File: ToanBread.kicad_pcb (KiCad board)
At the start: 2 copper layers, 53.3 x 101.6 mm, 32 parts, among them J1 PJ-059A, J2 AUDIO_IN, J3 VBIAS_OUT, J4 9V_OUT, J5 AUDIO_OUT, J6 EFF_OUT, J7 EFF_IN, U1 LM4562NA

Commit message: First pass at pcb layout
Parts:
- moved R6 59.3 mm to (134.6, 127.0), turned to 180 degrees
- moved C1 50.8 mm to (132.1, 114.3)
- moved C2 45.7 mm to (132.1, 61.0)
- moved C6 45.7 mm to (160.0, 78.7)
- moved J6 45.7 mm to (132.1, 50.8)
- moved J7 45.7 mm to (160.0, 50.8)
- moved R10 45.7 mm to (149.9, 68.6)
- moved R2 45.7 mm to (149.9, 91.4)
- moved R8 45.7 mm to (149.9, 86.4)
- moved S1 45.7 mm to (132.3, 137.2)
- moved BT1 45.7 mm to (121.9, 58.4)
- moved C4 45.7 mm to (134.6, 86.4)
- moved C5 45.7 mm to (165.1, 88.9)
- moved D1 45.7 mm to (124.5, 121.9)
- moved D3 45.7 mm to (152.4, 61.0)
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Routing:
- net BUF2_{OUT}: track 0.00 -> 84.1 mm
- net Net-(BT1--): track 0.00 -> 63.0 mm
- net BUF1_{IN}: track 0.00 -> 56.4 mm
- net Net-(J7-Pin_1): track 0.00 -> 54.2 mm
- net SIG: track 0.00 -> 49.1 mm
- net Net-(J6-Pin_1): track 0.00 -> 43.5 mm
- net Net-(R10-Pad2): track 0.00 -> 31.1 mm
- net Net-(J5-Pad2): track 0.00 -> 29.0 mm
- net Net-(R7-Pad1): track 0.00 -> 22.3 mm
- net Net-(C2-Pad1): track 0.00 -> 21.3 mm
- net Net-(D1-K): track 0.00 -> 21.1 mm
- net Net-(BT1-+): track 0.00 -> 20.0 mm
- net Net-(C4-Pad2): track 0.00 -> 16.9 mm
- net Net-(J3-Pin_2): track 0.00 -> 16.2 mm
- net 4V5: track 0.00 -> 15.2 mm
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- added copper zone on B.Cu, net GND
- added copper zone on F.Cu, net GND
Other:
- board size 53.3 x 101.6 mm -> 53.3 x 99.1 mm

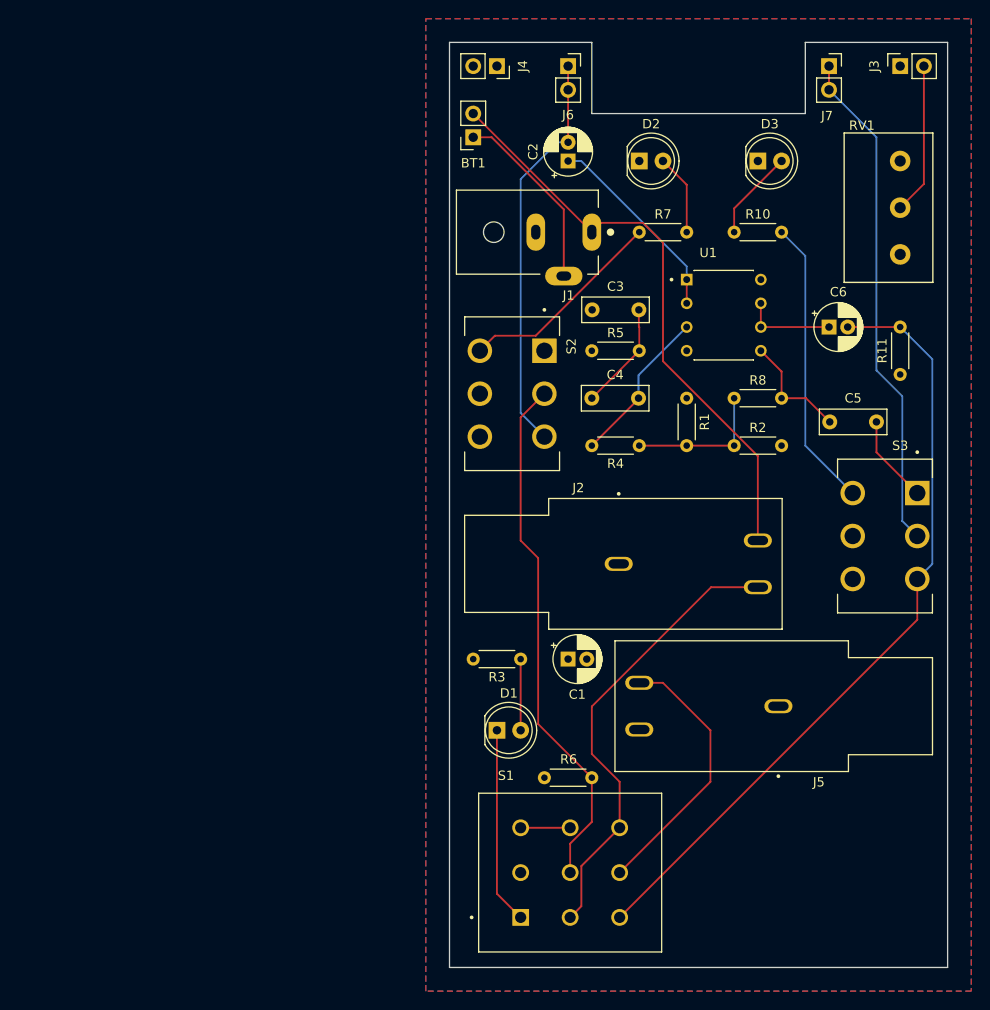
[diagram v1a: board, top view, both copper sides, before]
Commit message: Add info and logo to silkscreen
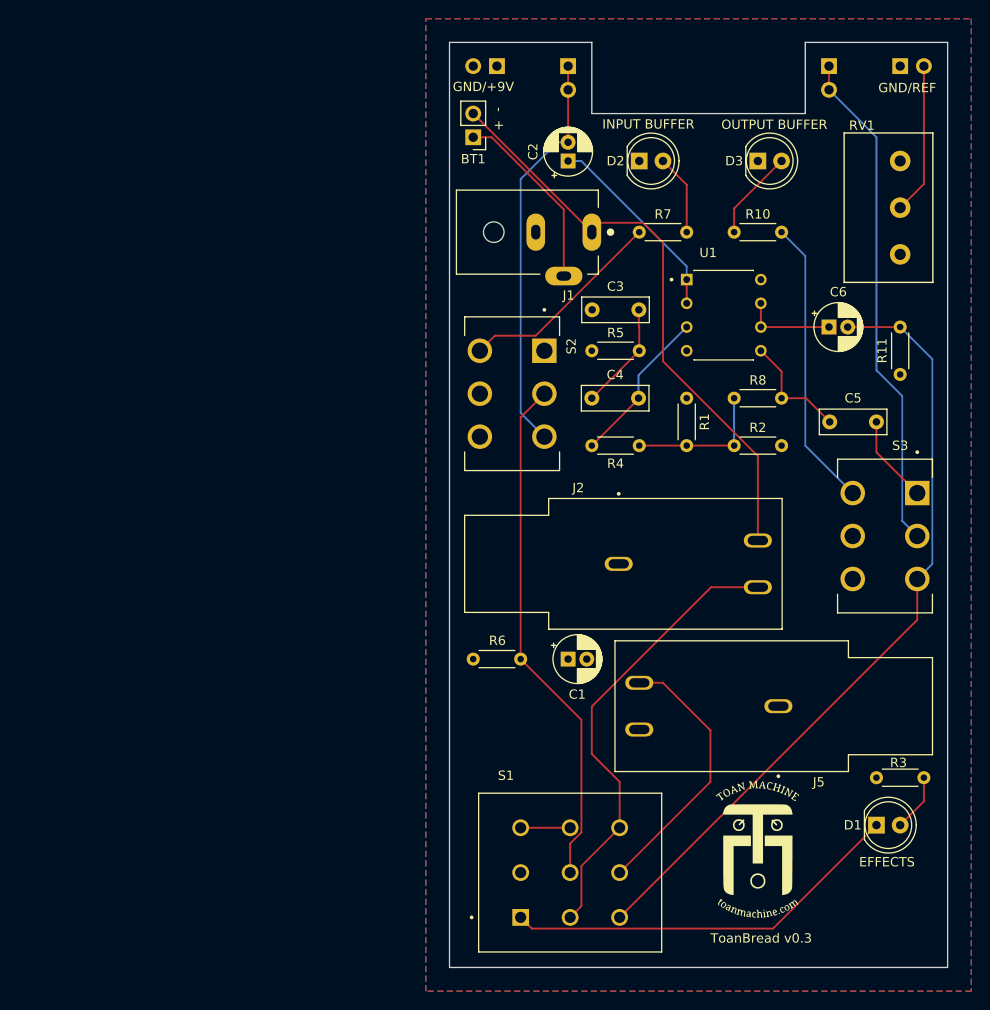
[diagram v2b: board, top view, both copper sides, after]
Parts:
- added G***: LOGO, ProjectSpecific:ToanMachineLogo, F.Cu at (152.4, 134.6)
- BT1: footprint Connector_PinSocket_2.54mm:PinSocket_1x02_P2.54mm_Vertical -> Connector_PinHeader_2.54mm:PinHeader_1x02_P2.54mm_Vertical
- J3, J4, J6, J7: footprint Connector_PinSocket_2.54mm:PinSocket_1x02_P2.54mm_Vertical -> Connector_PinHeader_2.54mm:PinHeader_1x02_P2.54mm_Vertical; moved to B.Cu
- moved R3 45.0 mm to (170.2, 127.0)
- moved D1 41.9 mm to (165.1, 132.1)
- moved R6 14.8 mm to (127.0, 114.3)
- turned J3 to -90 degrees
- turned J4 to 90 degrees
- turned J6 to 180 degrees
- turned J7 to 180 degrees
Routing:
- net Net-(D1-K): track 21.1 -> 43.2 mm
- net Net-(D1-A): track 7.62 -> 6.13 mm
- net BUF1_{IN}: track 56.4 -> 55.5 mm
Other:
- board text added: "- +"
- board text added: "EFFECTS"
- board text added: "GND/+9V"
- board text added: "GND/REF"
- board text added: "INPUT BUFFER"
- board text added: "OUTPUT BUFFER"
- board text added: "ToanBread v0.3"

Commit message: Final updates to the v0.3 board
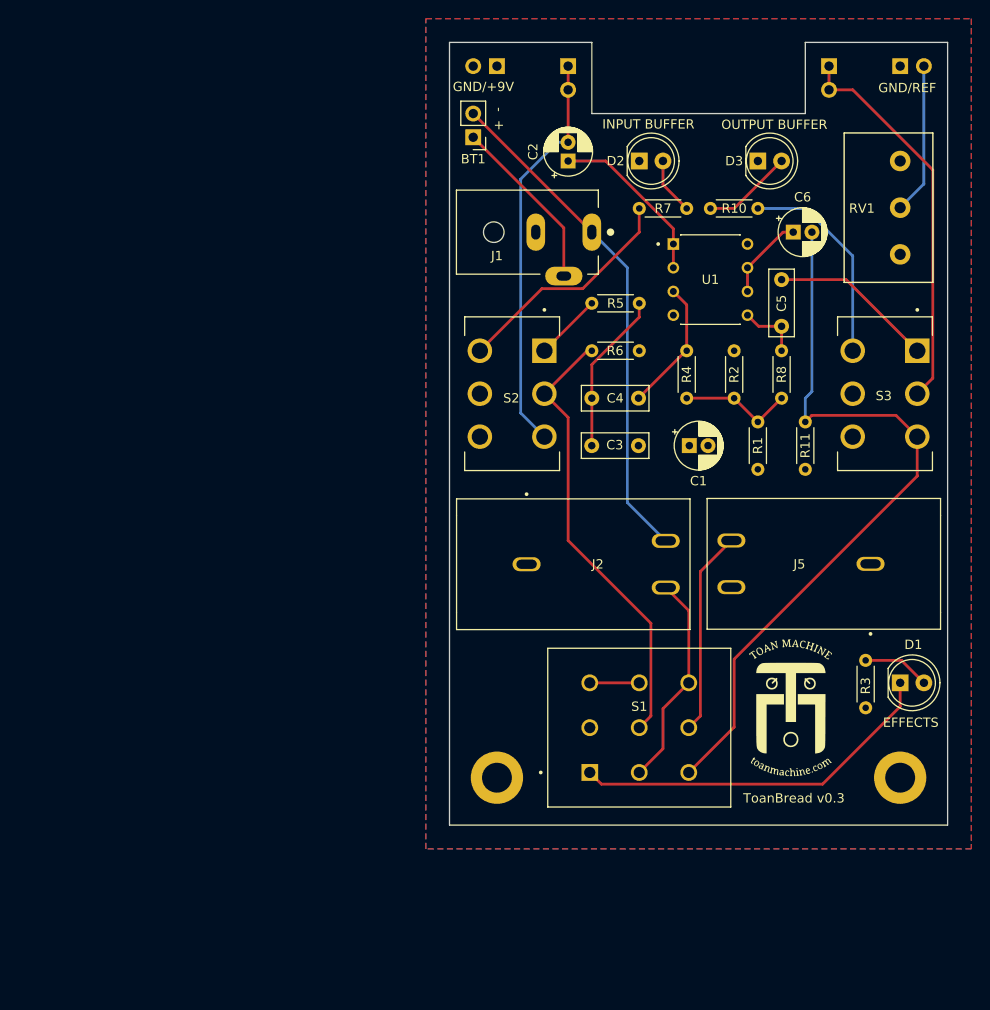
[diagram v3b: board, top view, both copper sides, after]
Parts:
- added MHL: MountingHole_3.2mm_M3_DIN965_Pad, MountingHole:MountingHole_3.2mm_M3_DIN965_Pad, F.Cu at (124.5, 127.0)
- added MHR: MountingHole_3.2mm_M3_DIN965_Pad, MountingHole:MountingHole_3.2mm_M3_DIN965_Pad, F.Cu at (167.6, 127.0)
- moved R6 33.9 mm to (134.6, 81.3), turned to 0 degrees
- moved C1 26.3 mm to (145.1, 91.4)
- moved C5 18.3 mm to (154.9, 73.7), turned to -90 degrees
- moved J5 18.2 mm to (164.5, 104.1)
- moved S1 17.2 mm to (139.7, 121.6)
- moved G*** 15.6 mm to (155.9, 119.5)
- moved D1 15.5 mm to (167.6, 116.8)
- moved C3 15.4 mm to (139.6, 91.4), turned to 180 degrees
- moved S3 15.2 mm to (166.0, 85.9)
- moved R11 14.4 mm to (157.5, 94.0)
- moved R3 14.0 mm to (163.9, 114.4), turned to -90 degrees
- moved C6 10.9 mm to (156.2, 68.6)
- moved R1 10.8 mm to (152.4, 94.0), turned to 90 degrees
- moved J2 9.87 mm to (127.6, 104.1)
- moved R4 7.18 mm to (144.8, 86.4), turned to 90 degrees
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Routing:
- net SIG: track 49.1 -> 23.0 mm
- net Net-(J7-Pin_1): track 54.2 -> 41.9 mm
- net Net-(BT1--): track 63.0 -> 54.3 mm
- net Net-(R10-Pad2): track 31.1 -> 22.4 mm
- net Net-(C5-Pad1): track 9.43 -> 17.7 mm
- net BUF1_{IN}: track 55.5 -> 48.0 mm
- net Net-(R5-Pad1): track 0.00 -> 7.18 mm
- net Net-(J5-Pad2): track 29.0 -> 21.9 mm
- net Net-(C3-Pad2): track 11.6 -> 17.3 mm
- net Net-(C5-Pad2): track 12.2 -> 6.76 mm
- net BUF2_{OUT}: track 84.1 -> 79.9 mm
- net Net-(D1-K): track 43.2 -> 39.7 mm
- net 4V5: track 15.2 -> 12.3 mm
- net Net-(C2-Pad1): track 21.3 -> 18.5 mm
- net Net-(C4-Pad2): track 16.9 -> 14.2 mm
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- added copper zone on F.Cu, net +9V
- removed copper zone on F.Cu, net GND
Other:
- board size 53.3 x 99.1 mm -> 53.3 x 83.8 mm
